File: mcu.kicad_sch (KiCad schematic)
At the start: 11 parts, among them J3 Conn_02x05_Odd_Even, SW2 SW_Push, U4 E73-2G4M04S-52832

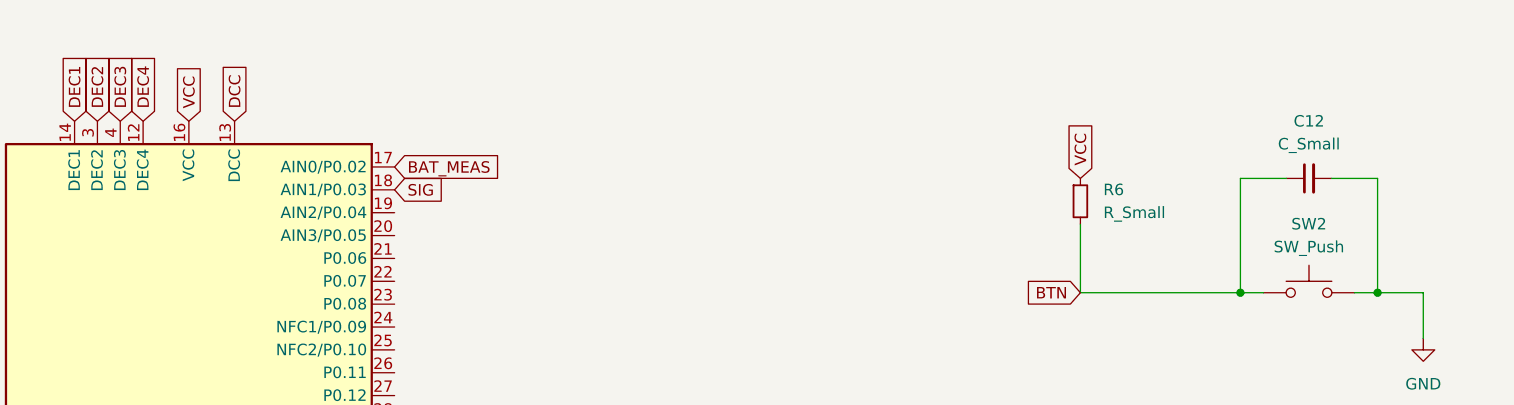
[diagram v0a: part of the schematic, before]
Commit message: Fix power on debug connector
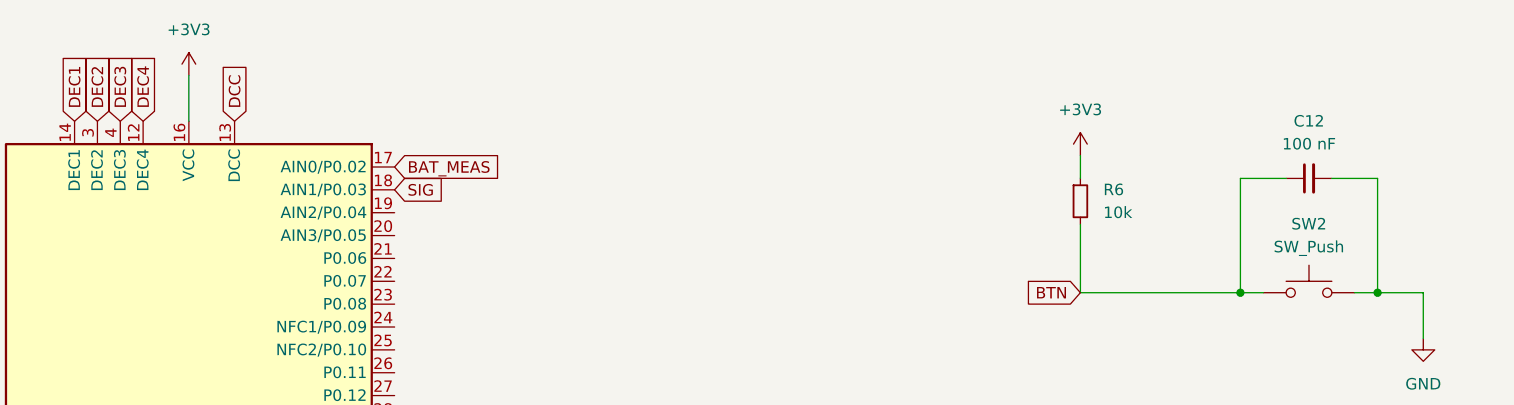
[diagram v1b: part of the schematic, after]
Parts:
- C12: value C_Small -> 100 nF
- R6: value R_Small -> 10k
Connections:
- net VCC is gone; now on net +3V3: R6.1, U4.16 (VCC)

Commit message: fix c12 footprint
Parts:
- C12: footprint LED_SMD:LED_0805_2012Metric -> Capacitor_SMD:C_0805_2012Metric
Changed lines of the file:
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@@
 			)
 		)
-		(property "Footprint" "LED_SMD:LED_0805_2012Metric"
+		(property "Footprint" "Capacitor_SMD:C_0805_2012Metric"
 			(at 228.6 58.42 0)
 			(effects
